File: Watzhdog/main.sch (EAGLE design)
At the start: 44 parts, among them CN1 MICROUSB(MC-5F-02), IC1 C8051F381-GM, IC3 N25Q512A, IC6 MPU-9250, U1 MCP73831, U2 TPS61201

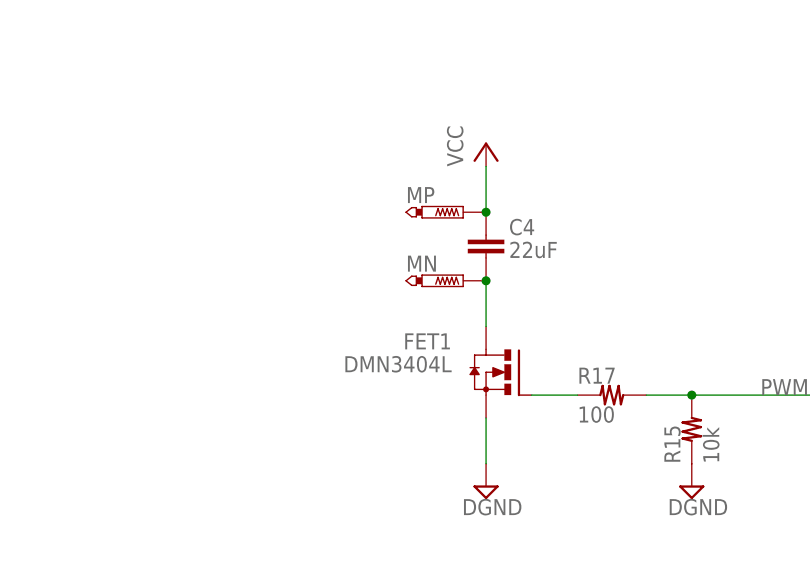
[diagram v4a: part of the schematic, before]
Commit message: Modified parts position
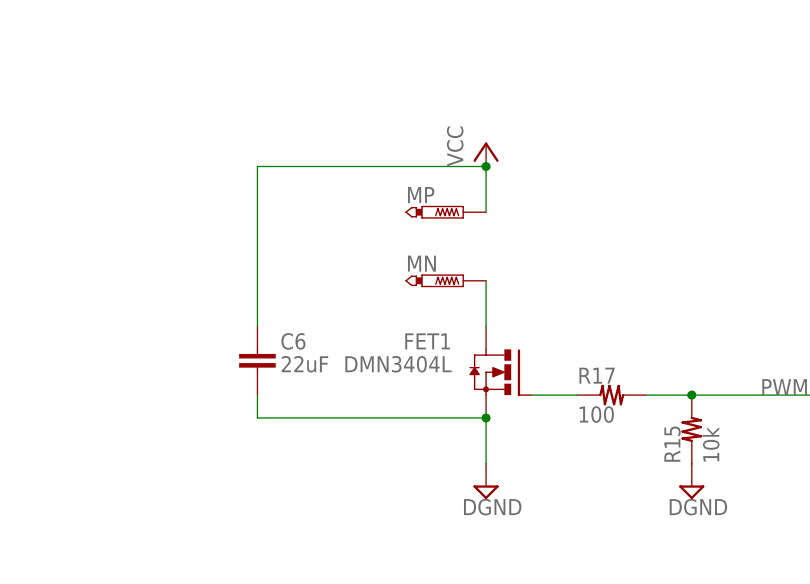
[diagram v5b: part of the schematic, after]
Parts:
- removed C4: 22uF, CH_passive:CAP0805
- added C6: 22uF, CH_passive:CAP0805
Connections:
- net DGND: now also C6.2
- net N$10: no longer C4.2
- net VCC: now also C6.1; no longer C4.1
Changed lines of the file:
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@@
 <part name="C2" library="CH_passive" deviceset="CAP" device="0805" value="22uF"/>
 <part name="R1" library="reg,cap" deviceset="R-" device="1005" value="1k (Optional)"/>
-<part name="C4" library="CH_passive" deviceset="CAP" device="0805" value="22uF"/>
+<part name="C6" library="CH_passive" deviceset="CAP" device="0805" value="22uF"/>
 </parts>
 <sheets>
@@
 </instance>
 <instance part="R1" gate="G$1" x="210.82" y="43.18" rot="R90"/>
-<instance part="C4" gate="G$1" x="353.06" y="-60.96" smashed="yes">
-<attribute name="NAME" x="355.6" y="-58.42" size="1.778" layer="95"/>
-<attribute name="VALUE" x="355.6" y="-60.96" size="1.778" layer="96"/>
+<instance part="C6" gate="G$1" x="327.66" y="-73.66" smashed="yes">
+<attribute name="NAME" x="330.2" y="-71.12" size="1.778" layer="95"/>
+<attribute name="VALUE" x="330.2" y="-73.66" size="1.778" layer="96"/>
 </instance>
 </instances>
@@
 <pinref part="SUPPLY5" gate="G$1" pin="DGND"/>
 <wire x1="353.06" y1="-78.74" x2="353.06" y2="-83.82" width="0.1524" layer="91"/>
+<pinref part="C6" gate="G$1" pin="2"/>
+<wire x1="353.06" y1="-78.74" x2="327.66" y2="-78.74" width="0.1524" layer="91"/>
+<wire x1="327.66" y1="-78.74" x2="327.66" y2="-76.2" width="0.1524" layer="91"/>
+<junction x="353.06" y="-78.74"/>
 </segment>
 <segment>
@@
 <wire x1="353.06" y1="-55.88" x2="353.06" y2="-50.8" width="0.1524" layer="91"/>
 <pinref part="+3V3" gate="VCC" pin="VCC"/>
-<pinref part="C4" gate="G$1" pin="1"/>
-<junction x="353.06" y="-55.88"/>
+<pinref part="C6" gate="G$1" pin="1"/>
+<wire x1="327.66" y1="-68.58" x2="327.66" y2="-50.8" width="0.1524" layer="91"/>
+<wire x1="327.66" y1="-50.8" x2="353.06" y2="-50.8" width="0.1524" layer="91"/>
+<junction x="353.06" y="-50.8"/>
 </segment>
 </net>
@@
 <pinref part="FET1" gate="G$1" pin="D"/>
 <wire x1="353.06" y1="-63.5" x2="353.06" y2="-68.58" width="0.1524" layer="91"/>
-<pinref part="C4" gate="G$1" pin="2"/>
-<junction x="353.06" y="-63.5"/>
-</segment>
-</net>
+</segment>
+</net>

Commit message: Modified parts position
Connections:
- net N$15: now also IC1G$1.P2.6; no longer IC1G$1.P2.7
- net N$5: now also IC1G$1.P2.7; no longer IC1G$1.P0.1
- net N$7: now also IC1G$1.P2.1; no longer IC1G$1.P0.0
- net PWM: now also IC1G$1.P0.2/XTAL1; no longer IC1G$1.P2.6
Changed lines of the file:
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@@
 <segment>
 <wire x1="375.92" y1="-15.24" x2="375.92" y2="-10.16" width="0.1524" layer="91"/>
-<wire x1="393.7" y1="33.02" x2="393.7" y2="-10.16" width="0.1524" layer="91"/>
-<wire x1="393.7" y1="-10.16" x2="375.92" y2="-10.16" width="0.1524" layer="91"/>
+<wire x1="396.24" y1="-10.16" x2="375.92" y2="-10.16" width="0.1524" layer="91"/>
 <pinref part="R9" gate="G$1" pin="P$2"/>
-<pinref part="IC1" gate="G$1" pin="P2.7"/>
 <pinref part="JP2" gate="G$1" pin="1"/>
 <wire x1="375.92" y1="-10.16" x2="375.92" y2="-2.54" width="0.1524" layer="91"/>
 <junction x="375.92" y="-10.16"/>
+<pinref part="IC1" gate="G$1" pin="P2.6"/>
+<wire x1="396.24" y1="33.02" x2="396.24" y2="-10.16" width="0.1524" layer="91"/>
 </segment>
 </net>
@@
 <net name="N$5" class="0">
 <segment>
-<pinref part="IC1" gate="G$1" pin="P0.1"/>
-<wire x1="373.38" y1="66.04" x2="213.36" y2="66.04" width="0.1524" layer="91"/>
+<wire x1="248.92" y1="66.04" x2="213.36" y2="66.04" width="0.1524" layer="91"/>
 <wire x1="213.36" y1="66.04" x2="213.36" y2="86.36" width="0.1524" layer="91"/>
 <wire x1="213.36" y1="86.36" x2="195.58" y2="86.36" width="0.1524" layer="91"/>
 <pinref part="R16" gate="G$1" pin="P$1"/>
+<pinref part="IC1" gate="G$1" pin="P2.7"/>
+<wire x1="393.7" y1="33.02" x2="393.7" y2="2.54" width="0.1524" layer="91"/>
+<wire x1="393.7" y1="2.54" x2="353.06" y2="2.54" width="0.1524" layer="91"/>
+<wire x1="353.06" y1="2.54" x2="353.06" y2="-7.62" width="0.1524" layer="91"/>
+<wire x1="353.06" y1="-7.62" x2="248.92" y2="-7.62" width="0.1524" layer="91"/>
+<wire x1="248.92" y1="-7.62" x2="248.92" y2="66.04" width="0.1524" layer="91"/>
 </segment>
 </net>
@@
 <net name="N$7" class="0">
 <segment>
-<pinref part="IC1" gate="G$1" pin="P0.0"/>
-<wire x1="373.38" y1="63.5" x2="210.82" y2="63.5" width="0.1524" layer="91"/>
+<wire x1="360.68" y1="63.5" x2="210.82" y2="63.5" width="0.1524" layer="91"/>
 <wire x1="210.82" y1="63.5" x2="210.82" y2="81.28" width="0.1524" layer="91"/>
 <wire x1="210.82" y1="81.28" x2="203.2" y2="81.28" width="0.1524" layer="91"/>
@@
 <wire x1="203.2" y1="35.56" x2="203.2" y2="81.28" width="0.1524" layer="91"/>
 <junction x="203.2" y="81.28"/>
+<pinref part="IC1" gate="G$1" pin="P2.1"/>
+<wire x1="421.64" y1="48.26" x2="426.72" y2="48.26" width="0.1524" layer="91"/>
+<wire x1="426.72" y1="48.26" x2="426.72" y2="104.14" width="0.1524" layer="91"/>
+<wire x1="426.72" y1="104.14" x2="360.68" y2="104.14" width="0.1524" layer="91"/>
+<wire x1="360.68" y1="104.14" x2="360.68" y2="63.5" width="0.1524" layer="91"/>
 </segment>
 </net>
@@
 <segment>
 <pinref part="R15" gate="G$1" pin="P$2"/>
-<pinref part="IC1" gate="G$1" pin="P2.6"/>
 <wire x1="370.84" y1="-76.2" x2="375.92" y2="-76.2" width="0.1524" layer="91"/>
-<wire x1="396.24" y1="33.02" x2="396.24" y2="-76.2" width="0.1524" layer="91"/>
-<wire x1="396.24" y1="-76.2" x2="375.92" y2="-76.2" width="0.1524" layer="91"/>
 <junction x="375.92" y="-76.2"/>
 <label x="383.54" y="-76.2" size="1.778" layer="95"/>
 <pinref part="R17" gate="G$1" pin="P$2"/>
-</segment>
-</net>
+<wire x1="393.7" y1="-76.2" x2="375.92" y2="-76.2" width="0.1524" layer="91"/>
+<pinref part="IC1" gate="G$1" pin="P0.2/XTAL1"/>
+<wire x1="393.7" y1="-30.48" x2="393.7" y2="-76.2" width="0.1524" layer="91"/>
+<wire x1="388.62" y1="81.28" x2="345.44" y2="81.28" width="0.1524" layer="91"/>
+<wire x1="345.44" y1="81.28" x2="345.44" y2="-30.48" width="0.1524" layer="91"/>
+<wire x1="345.44" y1="-30.48" x2="393.7" y2="-30.48" width="0.1524" layer="91"/>
+</segment>
+</net>
